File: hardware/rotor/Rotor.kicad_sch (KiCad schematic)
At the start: 0 parts

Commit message: Pogo pin and schematic
Added the pogo pin footprint and model.
Updated the rotor schematic.
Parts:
- added J1, J2, J3, J4: POGO D2.0mm, TENG:PogoPin_D2.0mm, symbol Connector:Conn_01x01_Pin
- added J10, J11, J12, J5, J6, J7, J8, J9: TENG 10X10 8P, TENG:CONTACT_CIRCLE_10X10_8P, symbol Connector_Generic:Conn_01x01
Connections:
- new net: J2.1 (Pin_1), J7.1 (Pin_1), J8.1 (Pin_1)
- new net: J1.1 (Pin_1), J5.1 (Pin_1), J6.1 (Pin_1)
- new net: J10.1 (Pin_1), J3.1 (Pin_1), J9.1 (Pin_1)
- new net: J11.1 (Pin_1), J12.1 (Pin_1), J4.1 (Pin_1)

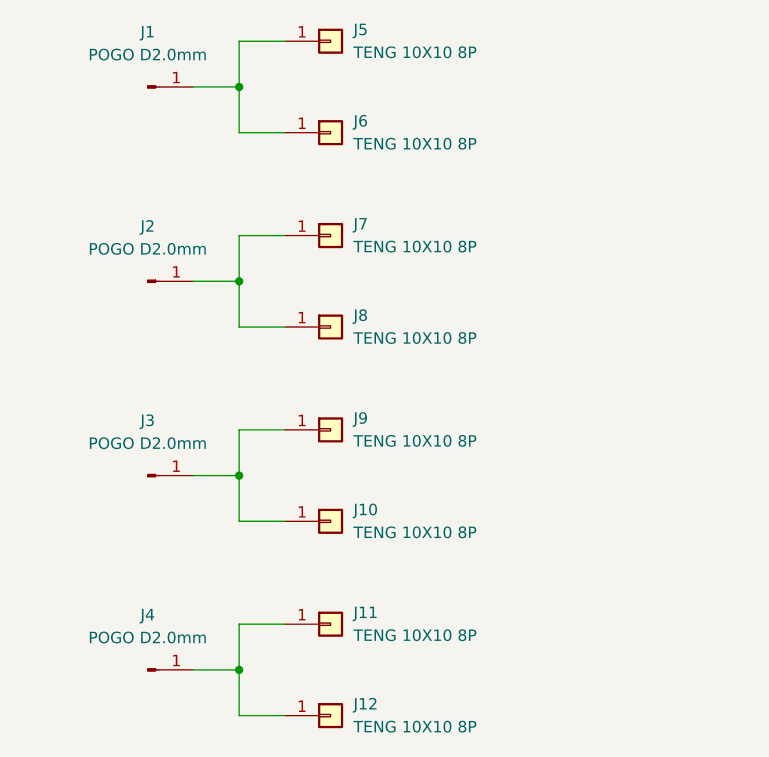
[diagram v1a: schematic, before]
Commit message: Generator layouts and footprints
Updated the TENG footprint library.
Updated the rotor and stator PCB layouts.
Generated new 3D models for the rotor and stator.
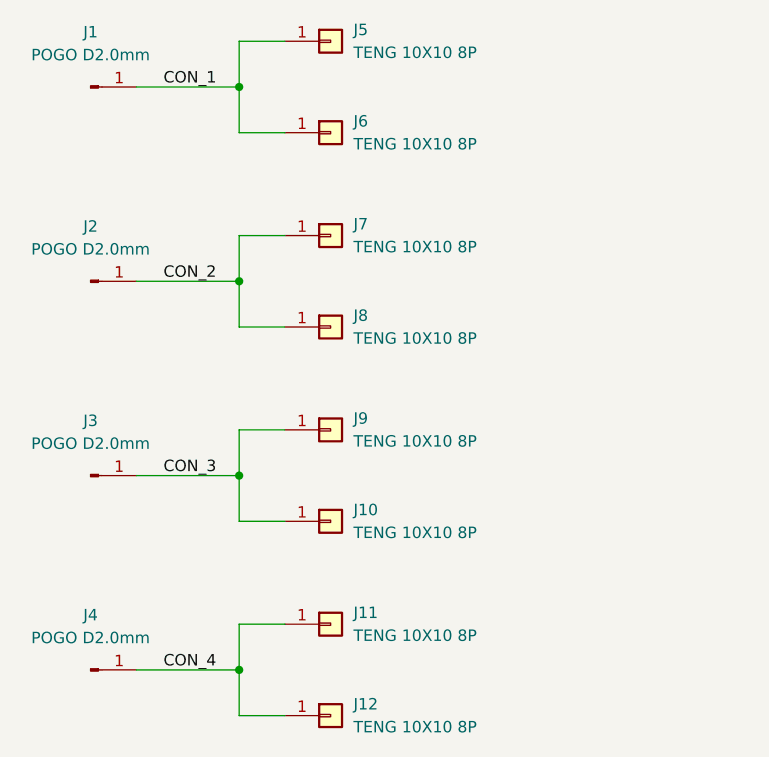
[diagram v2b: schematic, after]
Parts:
- J1, J2, J3, J4: footprint TENG:PogoPin_D2.0mm -> TENG:PogoPin_D2.0mm_JOIN
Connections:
- net CON_2: now reaches J2.1 (Pin_1), J7.1 (Pin_1), J8.1 (Pin_1)
- net CON_1: now reaches J1.1 (Pin_1), J5.1 (Pin_1), J6.1 (Pin_1)
- net CON_3: now reaches J10.1 (Pin_1), J3.1 (Pin_1), J9.1 (Pin_1)
- net CON_4: now reaches J11.1 (Pin_1), J12.1 (Pin_1), J4.1 (Pin_1)
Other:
- moved on the sheet: J1, J2, J3, J4
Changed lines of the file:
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@@
 	(wire
 		(pts
-			(xy 125.73 128.27) (xy 130.81 128.27)
+			(xy 119.38 128.27) (xy 130.81 128.27)
 		)
 		(stroke
@@
 	(wire
 		(pts
-			(xy 125.73 106.68) (xy 130.81 106.68)
+			(xy 119.38 106.68) (xy 130.81 106.68)
 		)
 		(stroke
@@
 	(wire
 		(pts
-			(xy 125.73 85.09) (xy 130.81 85.09)
+			(xy 119.38 85.09) (xy 130.81 85.09)
 		)
 		(stroke
@@
 	(wire
 		(pts
-			(xy 125.73 63.5) (xy 130.81 63.5)
+			(xy 119.38 63.5) (xy 130.81 63.5)
 		)
 		(stroke
@@
 			(width 0)
 			(type default)
+		)
+	)
+	(label "CON_3"
+		(at 128.27 106.68 180)
+		(effects
+			(font
+				(size 1.27 1.27)
+			)
+			(justify right bottom)
+		)
+	)
+	(label "CON_2"
+		(at 128.27 85.09 180)
+		(effects
+			(font
+				(size 1.27 1.27)
+			)
+			(justify right bottom)
+		)
+	)
+	(label "CON_4"
+		(at 128.27 128.27 180)
+		(effects
+			(font
+				(size 1.27 1.27)
+			)
+			(justify right bottom)
+		)
+	)
+	(label "CON_1"
+		(at 128.27 63.5 180)
+		(effects
+			(font
+				(size 1.27 1.27)
+			)
+			(justify right bottom)
 		)
 	)
@@
 		(exclude_from_sim no)
 		(in_bom no)
-		(on_board no)
-		(in_pos_files yes)
+		(on_board yes)
+		(in_pos_files no)
 		(dnp no)
 		(fields_autoplaced yes)
@@
 		(exclude_from_sim no)
 		(in_bom no)
-		(on_board no)
-		(in_pos_files yes)
+		(on_board yes)
+		(in_pos_files no)
 		(dnp no)
 		(fields_autoplaced yes)
@@
 	(symbol
 		(lib_id "Connector:Conn_01x01_Pin")
-		(at 120.65 106.68 0)
+		(at 114.3 106.68 0)
 		(unit 1)
 		(body_style 1)
@@
 		(dnp no)
 		(property "Reference" "J3"
-			(at 120.65 100.584 0)
+			(at 114.3 100.584 0)
 			(show_name no)
 			(do_not_autoplace no)
@@
 		)
 		(property "Value" "POGO D2.0mm"
-			(at 120.65 103.124 0)
-			(show_name no)
-			(do_not_autoplace no)
-			(effects
-				(font
-					(size 1.27 1.27)
-				)
-			)
-		)
-		(property "Footprint" "TENG:PogoPin_D2.0mm"
-			(at 120.65 106.68 0)
+			(at 114.3 103.124 0)
+			(show_name no)
+			(do_not_autoplace no)
+			(effects
+				(font
+					(size 1.27 1.27)
+				)
+			)
+		)
+		(property "Footprint" "TENG:PogoPin_D2.0mm_JOIN"
+			(at 114.3 106.68 0)
 			(hide yes)
 			(show_name no)
@@
 		)
 		(property "Datasheet" ""
-			(at 120.65 106.68 0)
+			(at 114.3 106.68 0)
 			(hide yes)
 			(show_name no)
@@
 		)
 		(property "Description" "Generic connector, single row, 01x01, script generated"
-			(at 120.65 106.68 0)
+			(at 114.3 106.68 0)
 			(hide yes)
 			(show_name no)
@@
 		)
 		(property "JLC Part" "C20612445"
-			(at 120.65 106.68 0)
+			(at 114.3 106.68 0)
 			(hide yes)
 			(show_name no)
@@
 		)
 		(property "Manufacturer Part" "YZ50315020R-03"
-			(at 120.65 106.68 0)
+			(at 114.3 106.68 0)
 			(hide yes)
 			(show_name no)
@@
 		(exclude_from_sim no)
 		(in_bom no)
-		(on_board no)
-		(in_pos_files yes)
+		(on_board yes)
+		(in_pos_files no)
 		(dnp no)
 		(fields_autoplaced yes)
@@
 		(exclude_from_sim no)
 		(in_bom no)
-		(on_board no)
-		(in_pos_files yes)
+		(on_board yes)
+		(in_pos_files no)
 		(dnp no)
 		(fields_autoplaced yes)
@@
 	(symbol
 		(lib_id "Connector:Conn_01x01_Pin")
-		(at 120.65 63.5 0)
+		(at 114.3 63.5 0)
 		(unit 1)
 		(body_style 1)
@@
 		(dnp no)
 		(property "Reference" "J1"
-			(at 120.65 57.404 0)
+			(at 114.3 57.404 0)
 			(show_name no)
 			(do_not_autoplace no)
@@
 		)
 		(property "Value" "POGO D2.0mm"
-			(at 120.65 59.944 0)
-			(show_name no)
-			(do_not_autoplace no)
-			(effects
-				(font
-					(size 1.27 1.27)
-				)
-			)
-		)
-		(property "Footprint" "TENG:PogoPin_D2.0mm"
-			(at 120.65 63.5 0)
+			(at 114.3 59.944 0)
+			(show_name no)
+			(do_not_autoplace no)
+			(effects
+				(font
+					(size 1.27 1.27)
+				)
+			)
+		)
+		(property "Footprint" "TENG:PogoPin_D2.0mm_JOIN"
+			(at 114.3 63.5 0)
 			(hide yes)
 			(show_name no)
@@
 		)
 		(property "Datasheet" ""
-			(at 120.65 63.5 0)
+			(at 114.3 63.5 0)
 			(hide yes)
 			(show_name no)
@@
 		)
 		(property "Description" "Generic connector, single row, 01x01, script generated"
-			(at 120.65 63.5 0)
+			(at 114.3 63.5 0)
 			(hide yes)
 			(show_name no)
@@
 		)
 		(property "JLC Part" "C20612445"
-			(at 120.65 63.5 0)
+			(at 114.3 63.5 0)
 			(hide yes)
 			(show_name no)
@@
 		)
 		(property "Manufacturer Part" "YZ50315020R-03"
-			(at 120.65 63.5 0)
+			(at 114.3 63.5 0)
 			(hide yes)
 			(show_name no)
@@
 		(exclude_from_sim no)
 		(in_bom no)
-		(on_board no)
-		(in_pos_files yes)
+		(on_board yes)
+		(in_pos_files no)
 		(dnp no)
 		(fields_autoplaced yes)
@@
 		(exclude_from_sim no)
 		(in_bom no)
-		(on_board no)
-		(in_pos_files yes)
+		(on_board yes)
+		(in_pos_files no)
 		(dnp no)
 		(fields_autoplaced yes)
@@
 		(exclude_from_sim no)
 		(in_bom no)
-		(on_board no)
-		(in_pos_files yes)
+		(on_board yes)
+		(in_pos_files no)
 		(dnp no)
 		(fields_autoplaced yes)
@@
 	(symbol
 		(lib_id "Connector:Conn_01x01_Pin")
-		(at 120.65 85.09 0)
+		(at 114.3 85.09 0)
 		(unit 1)
 		(body_style 1)
@@
 		(dnp no)
 		(property "Reference" "J2"
-			(at 120.65 78.994 0)
+			(at 114.3 78.994 0)
 			(show_name no)
 			(do_not_autoplace no)
@@
 		)
 		(property "Value" "POGO D2.0mm"
-			(at 120.65 81.534 0)
-			(show_name no)
-			(do_not_autoplace no)
-			(effects
-				(font
-					(size 1.27 1.27)
-				)
-			)
-		)
-		(property "Footprint" "TENG:PogoPin_D2.0mm"
-			(at 120.65 85.09 0)
+			(at 114.3 81.534 0)
+			(show_name no)
+			(do_not_autoplace no)
+			(effects
+				(font
+					(size 1.27 1.27)
+				)
+			)
+		)
+		(property "Footprint" "TENG:PogoPin_D2.0mm_JOIN"
+			(at 114.3 85.09 0)
 			(hide yes)
 			(show_name no)
@@
 		)
 		(property "Datasheet" ""
-			(at 120.65 85.09 0)
+			(at 114.3 85.09 0)
 			(hide yes)
 			(show_name no)
@@
 		)
 		(property "Description" "Generic connector, single row, 01x01, script generated"
-			(at 120.65 85.09 0)
+			(at 114.3 85.09 0)
 			(hide yes)
 			(show_name no)
@@
 		)
 		(property "JLC Part" "C20612445"
-			(at 120.65 85.09 0)
+			(at 114.3 85.09 0)
 			(hide yes)
 			(show_name no)
@@
 		)
 		(property "Manufacturer Part" "YZ50315020R-03"
-			(at 120.65 85.09 0)
+			(at 114.3 85.09 0)
 			(hide yes)
 			(show_name no)
@@
 	(symbol
 		(lib_id "Connector:Conn_01x01_Pin")
-		(at 120.65 128.27 0)
+		(at 114.3 128.27 0)
 		(unit 1)
 		(body_style 1)
@@
 		(dnp no)
 		(property "Reference" "J4"
-			(at 120.65 122.174 0)
+			(at 114.3 122.174 0)
 			(show_name no)
 			(do_not_autoplace no)
@@
 		)
 		(property "Value" "POGO D2.0mm"
-			(at 120.65 124.714 0)
-			(show_name no)
-			(do_not_autoplace no)
-			(effects
-				(font
-					(size 1.27 1.27)
-				)
-			)
-		)
-		(property "Footprint" "TENG:PogoPin_D2.0mm"
-			(at 120.65 128.27 0)
+			(at 114.3 124.714 0)
+			(show_name no)
+			(do_not_autoplace no)
+			(effects
+				(font
+					(size 1.27 1.27)
+				)
+			)
+		)
+		(property "Footprint" "TENG:PogoPin_D2.0mm_JOIN"
+			(at 114.3 128.27 0)
 			(hide yes)
 			(show_name no)
@@
 		)
 		(property "Datasheet" ""
-			(at 120.65 128.27 0)
+			(at 114.3 128.27 0)
 			(hide yes)
 			(show_name no)
@@
 		)
 		(property "Description" "Generic connector, single row, 01x01, script generated"
-			(at 120.65 128.27 0)
+			(at 114.3 128.27 0)
 			(hide yes)
 			(show_name no)
@@
 		)
 		(property "JLC Part" "C20612445"
-			(at 120.65 128.27 0)
+			(at 114.3 128.27 0)
 			(hide yes)
 			(show_name no)
@@
 		)
 		(property "Manufacturer Part" "YZ50315020R-03"
-			(at 120.65 128.27 0)
+			(at 114.3 128.27 0)
 			(hide yes)
 			(show_name no)
@@
 		(exclude_from_sim no)
 		(in_bom no)
-		(on_board no)
-		(in_pos_files yes)
+		(on_board yes)
+		(in_pos_files no)
 		(dnp no)
 		(fields_autoplaced yes)

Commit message: Pogo pin and production
Changed the pogo pins for ones with greater overall length, this takes into accout the thickness of the dielectric film.
Added the version information to the boards.
Built the production files.
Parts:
- added H1, H2, H3, H4: TOOLING, MountingHole:ToolingHole_1.152mm, symbol Mechanical:MountingHole
- J1, J2, J3, J4: JLC Part C20612445 -> C5157421; Manufacturer Part YZ50315020R-03 -> YZ203115028R-03
